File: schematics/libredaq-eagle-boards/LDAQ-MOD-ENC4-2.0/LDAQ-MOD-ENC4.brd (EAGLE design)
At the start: 25 parts, among them CON1 BOARD, IC1 5M240ZT100A5N, IC2 NCP164CSN180T1G, IC3 NXB0104PWJ, IC4 NXB0104PWJ, J1 SCREWTERMINAL-3.5MM-5, J2 SCREWTERMINAL-3.5MM-5, J3 70246-1004

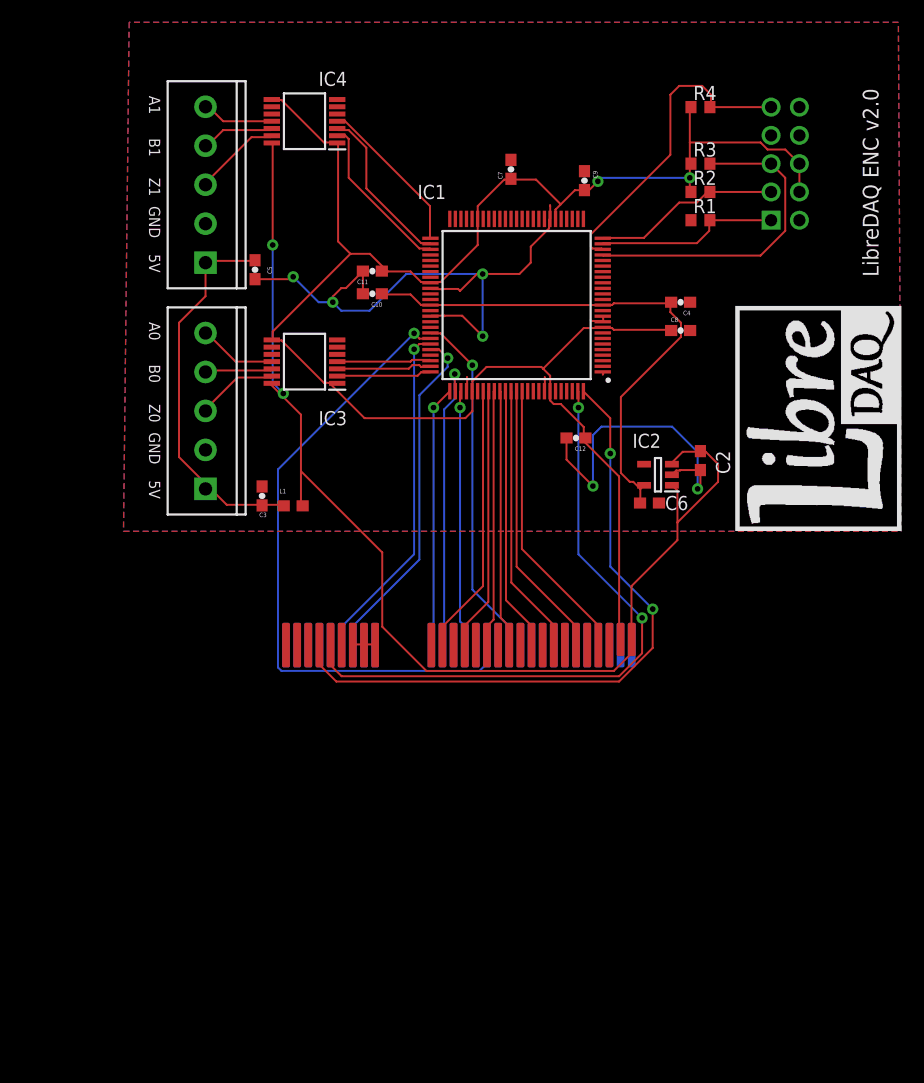
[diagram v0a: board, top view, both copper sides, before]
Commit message: Start upgrade to another FPGA
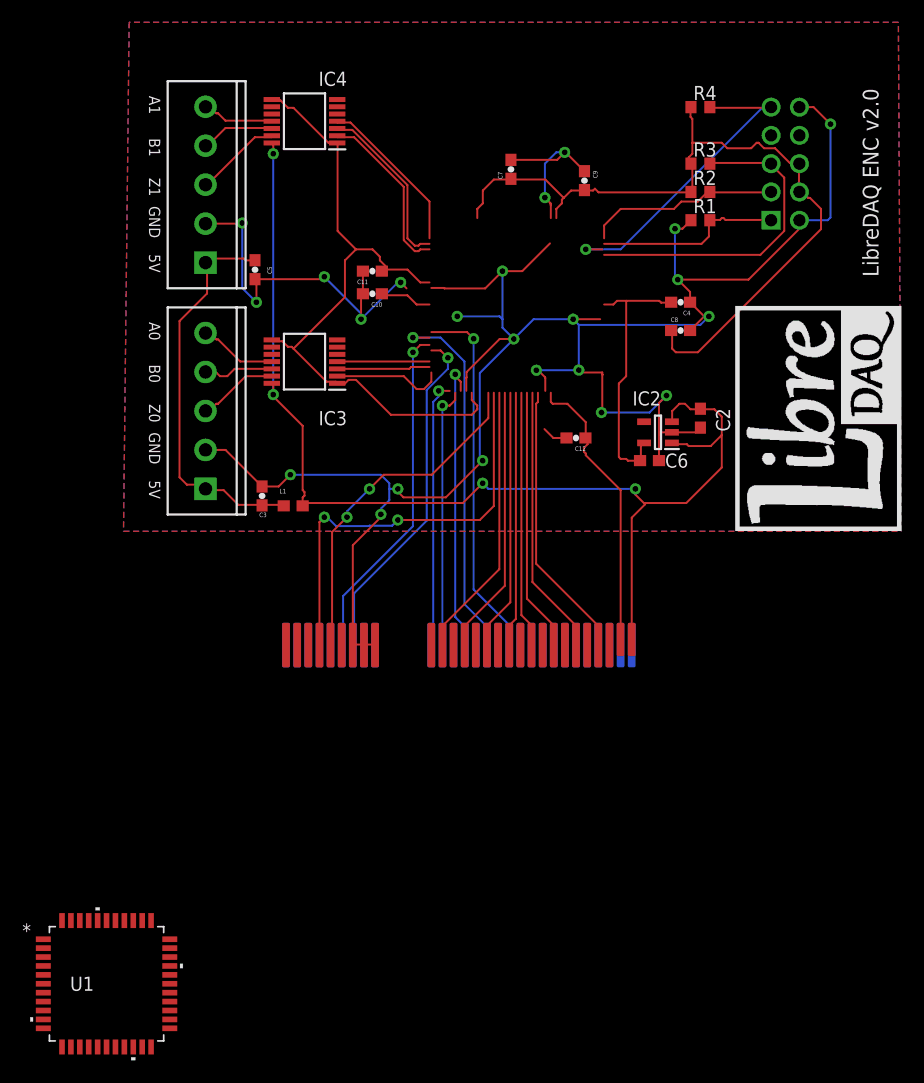
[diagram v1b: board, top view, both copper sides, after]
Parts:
- removed IC1: 5M240ZT100A5N, 5M240ZT100A5N:QFP50P1600X1600X120-100N
- added U1: XC2C64A-7VQG44I, XC2C64A-7VQG44I:44-VQFP_XIL
- moved C2 3.81 mm to (52.1, 24.1)
- moved C6 3.81 mm to (47.5, 20.3)
- moved IC2 3.81 mm to (48.3, 22.9)
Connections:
- new net GND_2: U1.4
- new net GND_3: U1.17
- new net VAUX: U1.35
- new net VCC: U1.15
- new net VCCIO1: U1.7
- new net VCCIO2: U1.26
- net +1.8V: no longer IC1.13, IC1.63
- net +3V3: no longer IC1.31, IC1.45, IC1.59, IC1.80, IC1.9, IC1.94
- net ALL_SLOTS_RESET: no longer IC1.76
- net CTRL0: no longer IC1.77
- net CTRL1: no longer IC1.78
- net CTRL2: no longer IC1.69
- net CTRL3: no longer IC1.68
- net DATA0: no longer IC1.82
- net DATA1: no longer IC1.83
- net DATA2: no longer IC1.84
- net DATA3: no longer IC1.85
- net DATA4: no longer IC1.86
- net DATA5: no longer IC1.87
- net DATA6: no longer IC1.88
- net DATA7: no longer IC1.89
- net ENC0A_3.3: no longer IC1.73
- net ENC0B_3.3: no longer IC1.74
- net ENC0Z_3.3: no longer IC1.75
- net ENC1A_3.3: no longer IC1.51
- net ENC1B_3.3: no longer IC1.52
- net ENC1Z_3.3: no longer IC1.53
- net GND: now also U1.25; no longer IC1.1, IC1.10, IC1.11, IC1.32, IC1.60, IC1.65, IC1.79, IC1.93
- net PNP_SCL/ENC_ADR0: no longer IC1.70
- net SLOT_ADDR0: no longer IC1.100
- net SLOT_ADDR1: no longer IC1.99
- net SLOT_PNP_SDA: no longer IC1.71
- net TCLK: no longer IC1.24
- net TDI: no longer IC1.23
- net TDO: no longer IC1.25
- net TMS: no longer IC1.22
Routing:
- net GND: track 91.5 -> 236.2 mm, vias 6 -> 23
- net SLOT_ADDR1: track 57.0 -> 31.1 mm
- net CTRL2: track 57.6 -> 33.3 mm
- net +1.8V: track 48.5 -> 29.0 mm
- net SLOT_ADDR0: track 59.2 -> 40.2 mm
- net +3V3: track 164.8 -> 157.9 mm, vias 2 -> 0
- net CTRL1: track 23.0 -> 26.4 mm
- net CTRL0: track 26.4 -> 23.5 mm
- net +5V: track 106.2 -> 104.7 mm, vias 2 -> 4
- net ENC0Z_3.3: track 8.52 -> 10.0 mm
- net CTRL3: track 31.5 -> 32.9 mm
- net ENC1Z_3.3: track 14.7 -> 15.5 mm
- net ENC1B_3.3: track 14.8 -> 15.6 mm
- net DATA4: track 23.8 -> 23.1 mm
- net DATA6: track 25.0 -> 24.3 mm
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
